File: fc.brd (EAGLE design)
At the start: 55 x 40 mm, 72 parts, among them IC1 BN055, J1 USBC, U1 LMZ21700, U2 ATMEGA2560-16AU100A-M, U4 FT230XQ, Y1 16MHz, Y2 32.768kHz

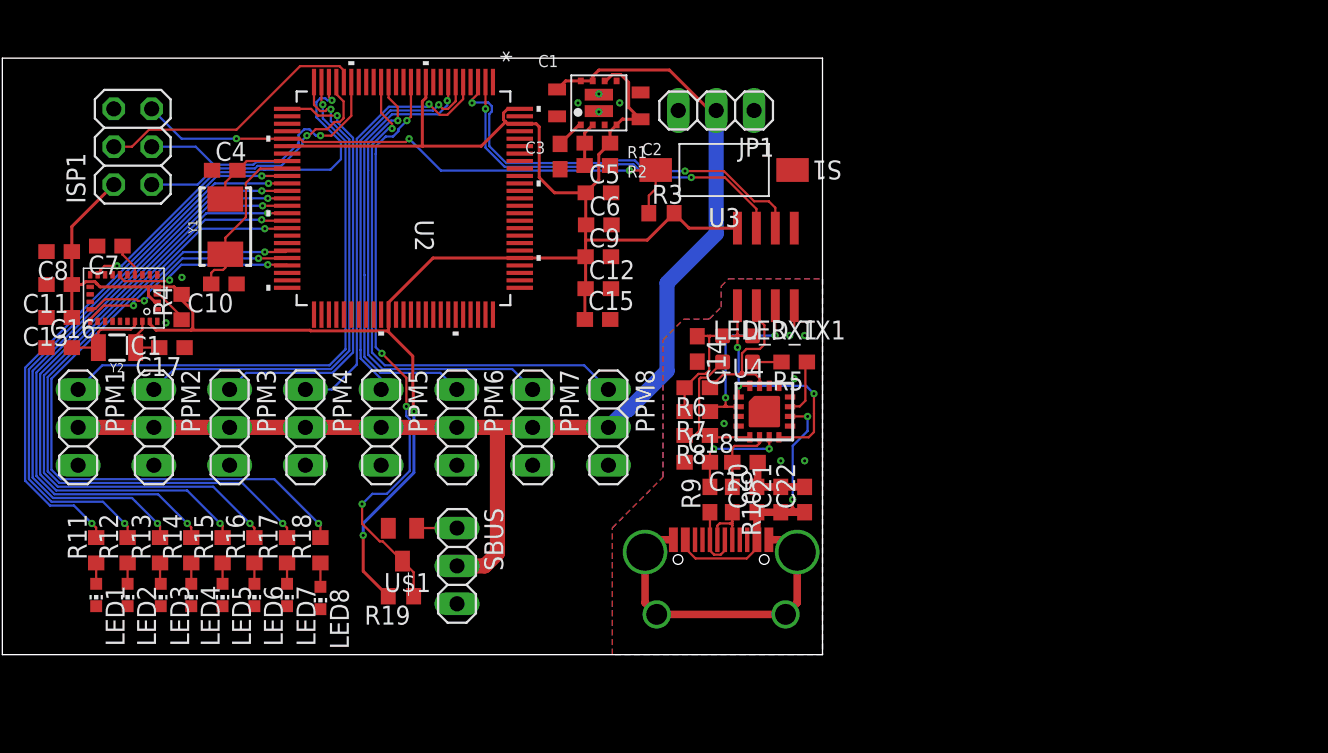
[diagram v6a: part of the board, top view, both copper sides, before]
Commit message: LED alignment
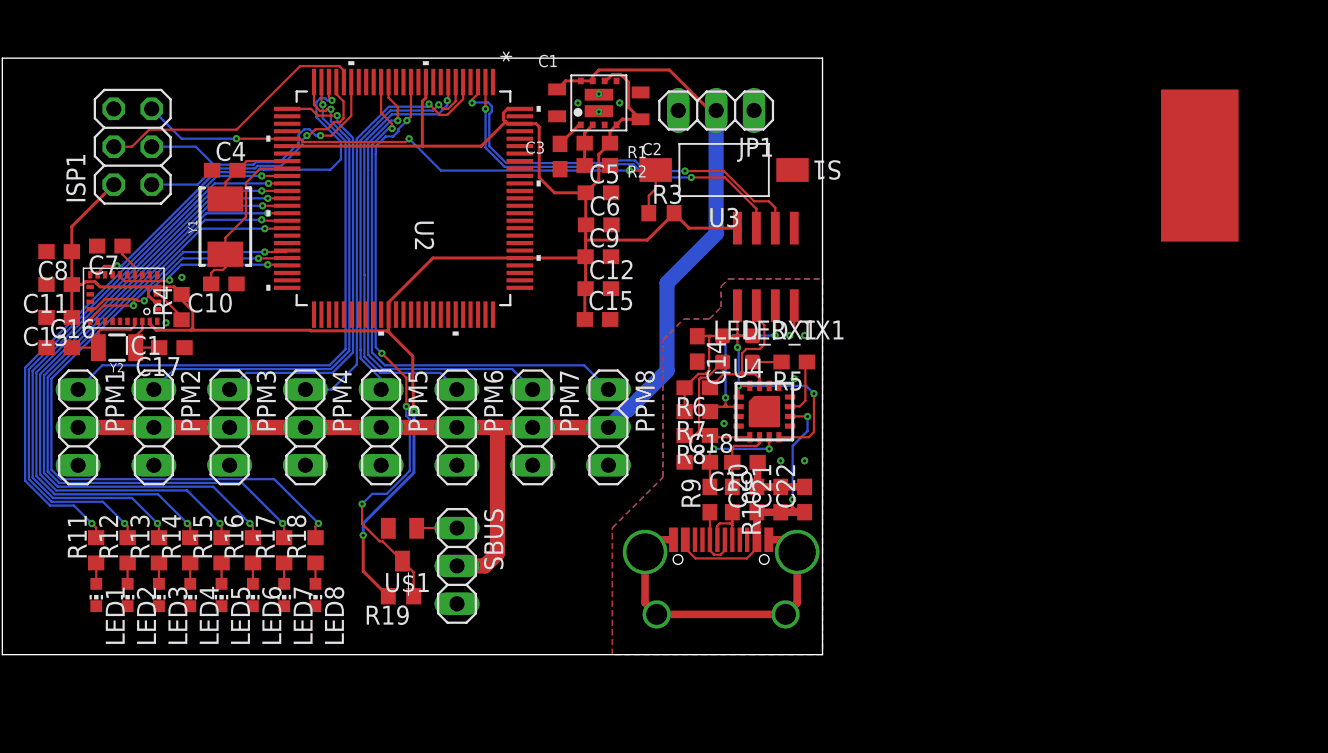
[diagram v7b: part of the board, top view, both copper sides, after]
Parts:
- moved LED8 0.39 mm to (21.0, 4.00)
- moved R18 0.33 mm to (21.0, 7.00)
- moved LED7 0.19 mm to (18.9, 4.00)
- moved R17 0.19 mm to (18.9, 7.00)
- moved LED3 0.12 mm to (10.5, 4.00)
- moved LED6 0.10 mm to (16.8, 4.00)
- moved R16 0.10 mm to (16.8, 7.00)
- moved R13 0.08 mm to (10.5, 7.00)
- moved LED4 0.07 mm to (12.6, 4.00)
- moved R14 0.07 mm to (12.6, 7.00)
- moved LED5 0.07 mm to (14.7, 4.00)
- moved R15 0.07 mm to (14.7, 7.00)
